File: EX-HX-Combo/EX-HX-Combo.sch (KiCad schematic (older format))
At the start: 46 parts, among them CN1 DB9 Male, J1 IDE_CONNECTOR, J200 Bus_Tandy_Plus_Through, J3 Bus_Tandy_Plus, SW1 SW_DIP_x10, U1 BIOS FLASH, U2 74HCT245, U3 1.8432 MHz, U4 DS1315, U5 AS6C4008-55PCN, U6 16550/16C550, U7 GD75232N, U8 GAL16V8, U9 GAL16V8, Y1 32.768 KHz

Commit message: Silkscreen work on EX-HX-Combo.
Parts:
- renumbered C99 to C10, C98 to C11, C10 to C12, C11 to C13, C12 to C14, C13 to C15, J3 to J2, J200 to J3
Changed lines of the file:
@@
 ~MEMR
 $Comp
-L 00Common:Bus_Tandy_Plus J3
+L 00Common:Bus_Tandy_Plus J2
 U 1 1 6039F90B
 P 2100 2750
-F 0 "J3" H 2100 4517 50  0000 C CNN
+F 0 "J2" H 2100 4517 50  0000 C CNN
 F 1 "Bus_Tandy_Plus" H 2100 4426 50  0000 C CNN
 F 2 "00Custom:TandyPlusSocket" H 2100 2750 50  0001 C CNN
@@
 UART_XIN
 $Comp
-L Device:CP C11
+L Device:CP C13
 U 1 1 60E3E53A
 P 13400 7700
-F 0 "C11" H 13518 7746 50  0000 L CNN
+F 0 "C13" H 13518 7746 50  0000 L CNN
 F 1 "100uF" H 13518 7655 50  0000 L CNN
 F 2 "Capacitor_Tantalum_SMD:CP_EIA-3528-15_AVX-H" H 13438 7550 50  0001 C CNN
@@
 $EndComp
 $Comp
-L Device:CP C12
+L Device:CP C14
 U 1 1 60D204F0
 P 13950 7700
-F 0 "C12" H 14068 7746 50  0000 L CNN
+F 0 "C14" H 14068 7746 50  0000 L CNN
 F 1 "10uF" H 14068 7655 50  0000 L CNN
 F 2 "Capacitor_Tantalum_SMD:CP_EIA-3528-15_AVX-H" H 13988 7550 50  0001 C CNN
@@
 $EndComp
 $Comp
-L Device:CP C13
+L Device:CP C15
 U 1 1 60D20522
 P 14450 7700
-F 0 "C13" H 14568 7746 50  0000 L CNN
+F 0 "C15" H 14568 7746 50  0000 L CNN
 F 1 "10uF" H 14568 7655 50  0000 L CNN
 F 2 "Capacitor_Tantalum_SMD:CP_EIA-3528-15_AVX-H" H 14488 7550 50  0001 C CNN
@@
 	5550 2850 5650 2850
 $Comp
-L 00Common:Bus_Tandy_Plus_For_Pass_Through J200
+L 00Common:Bus_Tandy_Plus_For_Pass_Through J3
 U 1 1 60D64444
 P 5050 2750
-F 0 "J200" H 5050 4517 50  0000 C CNN
+F 0 "J3" H 5050 4517 50  0000 C CNN
 F 1 "Bus_Tandy_Plus_Through" H 5050 4426 50  0000 C CNN
 F 2 "00Custom:TandyPlusSocket" H 5050 2750 50  0001 C CNN
@@
 $EndComp
 $Comp
-L Device:CP C10
+L Device:CP C12
 U 1 1 6117FB85
 P 12900 7700
-F 0 "C10" H 13018 7746 50  0000 L CNN
+F 0 "C12" H 13018 7746 50  0000 L CNN
 F 1 "100uF" H 13018 7655 50  0000 L CNN
 F 2 "Capacitor_Tantalum_SMD:CP_EIA-3528-15_AVX-H" H 12938 7550 50  0001 C CNN
@@
 $EndComp
 $Comp
-L Device:C C99
+L Device:C C10
 U 1 1 6131AD4C
 P 12050 8600
-F 0 "C99" H 12165 8646 50  0000 L CNN
+F 0 "C10" H 12165 8646 50  0000 L CNN
 F 1 "0.1uF" H 12165 8555 50  0000 L CNN
 F 2 "Capacitor_SMD:C_1206_3216Metric" H 12088 8450 50  0001 C CNN
@@
 $EndComp
 $Comp
-L Device:C C98
+L Device:C C11
 U 1 1 6143E0B4
 P 12550 8600
-F 0 "C98" H 12665 8646 50  0000 L CNN
+F 0 "C11" H 12665 8646 50  0000 L CNN
 F 1 "0.1uF" H 12665 8555 50  0000 L CNN
 F 2 "Capacitor_SMD:C_1206_3216Metric" H 12588 8450 50  0001 C CNN

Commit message: Lots of layout cleanup on EX-HX-Combo.
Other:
- note added: "MOUNTING"
- moved on the sheet: C10, C11, C12, C13, C14, C15, H1, H2, H3, H4, H5, H6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

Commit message: EX-HX-Combo: Getting close now...
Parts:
- U6: value 16550/16C550 -> 16C550
- Y1: value 32.768 KHz -> 32.768 kHz
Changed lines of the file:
@@
 P 2300 5500
 F 0 "Y1" V 2254 5631 50  0000 L CNN
-F 1 "32.768 KHz" V 2345 5631 50  0000 L CNN
+F 1 "32.768 kHz" V 2345 5631 50  0000 L CNN
 F 2 "Crystal:Crystal_C38-LF_D3.0mm_L8.0mm_Horizontal" H 2300 5500 50  0001 C CNN
 F 3 "~" H 2300 5500 50  0001 C CNN
@@
 P 2350 8850
 F 0 "U6" H 2450 10550 50  0000 C CNN
-F 1 "16550/16C550" H 2700 10450 50  0000 C CNN
+F 1 "16C550" H 2700 10450 50  0000 C CNN
 F 2 "Package_QFP:LQFP-48_7x7mm_P0.5mm" H 2350 8850 50  0001 C CIN
 F 3 "http://www.ti.com/lit/ds/symlink/pc16550d.pdf" H 2350 8850 50  0001 C CNN

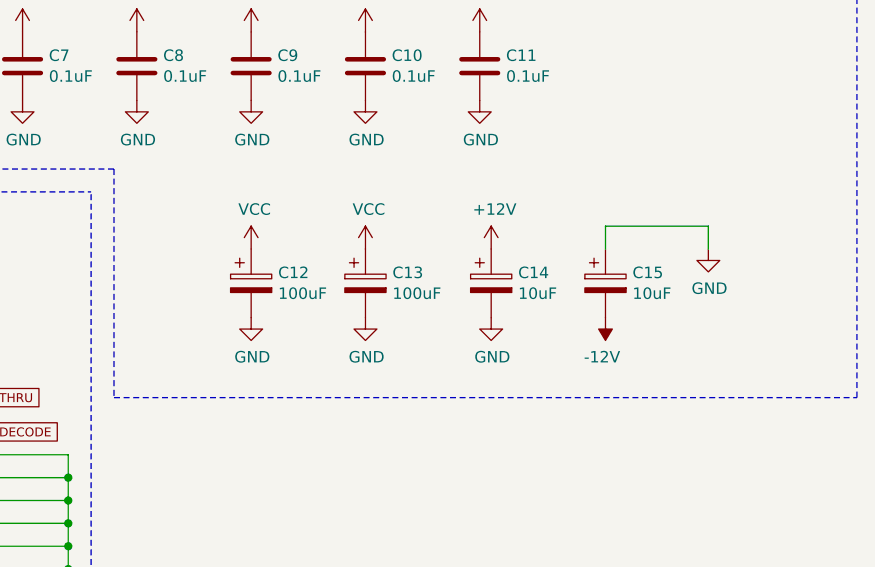
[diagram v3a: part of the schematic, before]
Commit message: EX-HX-Combo: Corrected Tantalum cap sizes, other minor changes.
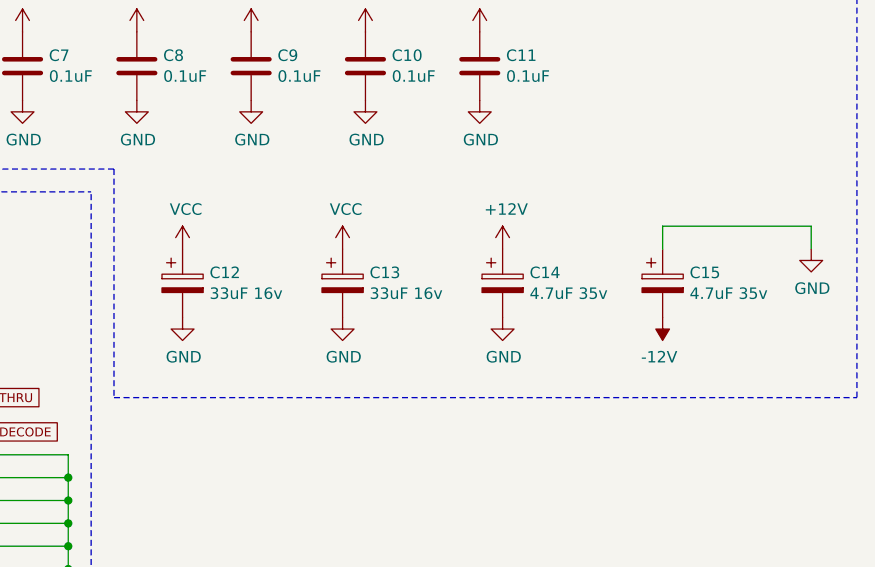
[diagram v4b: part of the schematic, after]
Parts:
- C12, C13: value 100uF -> 33uF 16v
- C14, C15: value 10uF -> 4.7uF 35v
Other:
- moved on the sheet: C12, C13, C14, C15
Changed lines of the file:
@@
 L power:VCC #PWR0121
 U 1 1 60E3DBDE
-P 12900 8500
-F 0 "#PWR0121" H 12900 8350 50  0001 C CNN
-F 1 "VCC" H 12915 8673 50  0000 C CNN
-F 2 "" H 12900 8500 50  0001 C CNN
-F 3 "" H 12900 8500 50  0001 C CNN
-	1    12900 8500
+P 12800 8500
+F 0 "#PWR0121" H 12800 8350 50  0001 C CNN
+F 1 "VCC" H 12815 8673 50  0000 C CNN
+F 2 "" H 12800 8500 50  0001 C CNN
+F 3 "" H 12800 8500 50  0001 C CNN
+	1    12800 8500
 	1    0    0    -1
 $EndComp
@@
 L power:GND #PWR0122
 U 1 1 60E3E530
-P 12900 8800
-F 0 "#PWR0122" H 12900 8550 50  0001 C CNN
-F 1 "GND" H 12905 8627 50  0000 C CNN
-F 2 "" H 12900 8800 50  0001 C CNN
-F 3 "" H 12900 8800 50  0001 C CNN
-	1    12900 8800
+P 12800 8800
+F 0 "#PWR0122" H 12800 8550 50  0001 C CNN
+F 1 "GND" H 12805 8627 50  0000 C CNN
+F 2 "" H 12800 8800 50  0001 C CNN
+F 3 "" H 12800 8800 50  0001 C CNN
+	1    12800 8800
 	1    0    0    -1
 $EndComp
@@
 Connection ~ 9100 10000
 Wire Wire Line
-	14400 8400 14400 8500
-Wire Wire Line
-	13950 8400 14400 8400
-Wire Wire Line
-	13950 8500 13950 8400
+	14850 8400 14850 8500
+Wire Wire Line
+	14200 8400 14850 8400
+Wire Wire Line
+	14200 8500 14200 8400
 $Comp
 L power:-12V #PWR0160
 U 1 1 60D20518
-P 13950 8800
-F 0 "#PWR0160" H 13950 8900 50  0001 C CNN
-F 1 "-12V" H 13965 8973 50  0000 C CNN
-F 2 "" H 13950 8800 50  0001 C CNN
-F 3 "" H 13950 8800 50  0001 C CNN
-	1    13950 8800
+P 14200 8800
+F 0 "#PWR0160" H 14200 8900 50  0001 C CNN
+F 1 "-12V" H 14215 8973 50  0000 C CNN
+F 2 "" H 14200 8800 50  0001 C CNN
+F 3 "" H 14200 8800 50  0001 C CNN
+	1    14200 8800
 	-1   0    0    1
 $EndComp
@@
 L power:+12V #PWR0159
 U 1 1 60D2050E
-P 13450 8500
-F 0 "#PWR0159" H 13450 8350 50  0001 C CNN
-F 1 "+12V" H 13465 8673 50  0000 C CNN
-F 2 "" H 13450 8500 50  0001 C CNN
-F 3 "" H 13450 8500 50  0001 C CNN
-	1    13450 8500
+P 13500 8500
+F 0 "#PWR0159" H 13500 8350 50  0001 C CNN
+F 1 "+12V" H 13515 8673 50  0000 C CNN
+F 2 "" H 13500 8500 50  0001 C CNN
+F 3 "" H 13500 8500 50  0001 C CNN
+	1    13500 8500
 	1    0    0    -1
 $EndComp
@@
 L power:GND #PWR0158
 U 1 1 60D20504
-P 14400 8500
-F 0 "#PWR0158" H 14400 8250 50  0001 C CNN
-F 1 "GND" H 14405 8327 50  0000 C CNN
-F 2 "" H 14400 8500 50  0001 C CNN
-F 3 "" H 14400 8500 50  0001 C CNN
-	1    14400 8500
+P 14850 8500
+F 0 "#PWR0158" H 14850 8250 50  0001 C CNN
+F 1 "GND" H 14855 8327 50  0000 C CNN
+F 2 "" H 14850 8500 50  0001 C CNN
+F 3 "" H 14850 8500 50  0001 C CNN
+	1    14850 8500
 	1    0    0    -1
 $EndComp
@@
 L power:GND #PWR0157
 U 1 1 60D204FA
-P 13450 8800
-F 0 "#PWR0157" H 13450 8550 50  0001 C CNN
-F 1 "GND" H 13455 8627 50  0000 C CNN
-F 2 "" H 13450 8800 50  0001 C CNN
-F 3 "" H 13450 8800 50  0001 C CNN
-	1    13450 8800
+P 13500 8800
+F 0 "#PWR0157" H 13500 8550 50  0001 C CNN
+F 1 "GND" H 13505 8627 50  0000 C CNN
+F 2 "" H 13500 8800 50  0001 C CNN
+F 3 "" H 13500 8800 50  0001 C CNN
+	1    13500 8800
 	1    0    0    -1
 $EndComp
@@
 L Device:CP C13
 U 1 1 60E3E53A
-P 12900 8650
-F 0 "C13" H 13018 8696 50  0000 L CNN
-F 1 "100uF" H 13018 8605 50  0000 L CNN
-F 2 "Capacitor_Tantalum_SMD:CP_EIA-3528-15_AVX-H" H 12938 8500 50  0001 C CNN
-F 3 "~" H 12900 8650 50  0001 C CNN
-	1    12900 8650
+P 12800 8650
+F 0 "C13" H 12918 8696 50  0000 L CNN
+F 1 "33uF 16v" H 12918 8605 50  0000 L CNN
+F 2 "Capacitor_Tantalum_SMD:CP_EIA-3528-15_AVX-H" H 12838 8500 50  0001 C CNN
+F 3 "~" H 12800 8650 50  0001 C CNN
+	1    12800 8650
 	1    0    0    -1
 $EndComp
@@
 L Device:CP C14
 U 1 1 60D204F0
-P 13450 8650
-F 0 "C14" H 13568 8696 50  0000 L CNN
-F 1 "10uF" H 13568 8605 50  0000 L CNN
-F 2 "Capacitor_Tantalum_SMD:CP_EIA-3528-15_AVX-H" H 13488 8500 50  0001 C CNN
-F 3 "~" H 13450 8650 50  0001 C CNN
-	1    13450 8650
+P 13500 8650
+F 0 "C14" H 13618 8696 50  0000 L CNN
+F 1 "4.7uF 35v" H 13618 8605 50  0000 L CNN
+F 2 "Capacitor_Tantalum_SMD:CP_EIA-3528-15_AVX-H" H 13538 8500 50  0001 C CNN
+F 3 "~" H 13500 8650 50  0001 C CNN
+	1    13500 8650
 	1    0    0    -1
 $EndComp
@@
 L Device:CP C15
 U 1 1 60D20522
-P 13950 8650
-F 0 "C15" H 14068 8696 50  0000 L CNN
-F 1 "10uF" H 14068 8605 50  0000 L CNN
-F 2 "Capacitor_Tantalum_SMD:CP_EIA-3528-15_AVX-H" H 13988 8500 50  0001 C CNN
-F 3 "~" H 13950 8650 50  0001 C CNN
-	1    13950 8650
+P 14200 8650
+F 0 "C15" H 14318 8696 50  0000 L CNN
+F 1 "4.7uF 35v" H 14318 8605 50  0000 L CNN
+F 2 "Capacitor_Tantalum_SMD:CP_EIA-3528-15_AVX-H" H 14238 8500 50  0001 C CNN
+F 3 "~" H 14200 8650 50  0001 C CNN
+	1    14200 8650
 	1    0    0    -1
 $EndComp
@@
 L power:VCC #PWR0171
 U 1 1 6117F173
-P 12400 8500
-F 0 "#PWR0171" H 12400 8350 50  0001 C CNN
-F 1 "VCC" H 12415 8673 50  0000 C CNN
-F 2 "" H 12400 8500 50  0001 C CNN
-F 3 "" H 12400 8500 50  0001 C CNN
-	1    12400 8500
+P 12100 8500
+F 0 "#PWR0171" H 12100 8350 50  0001 C CNN
+F 1 "VCC" H 12115 8673 50  0000 C CNN
+F 2 "" H 12100 8500 50  0001 C CNN
+F 3 "" H 12100 8500 50  0001 C CNN
+	1    12100 8500
 	1    0    0    -1
 $EndComp
@@
 L power:GND #PWR0172
 U 1 1 6117FB7B
-P 12400 8800
-F 0 "#PWR0172" H 12400 8550 50  0001 C CNN
-F 1 "GND" H 12405 8627 50  0000 C CNN
-F 2 "" H 12400 8800 50  0001 C CNN
-F 3 "" H 12400 8800 50  0001 C CNN
-	1    12400 8800
+P 12100 8800
+F 0 "#PWR0172" H 12100 8550 50  0001 C CNN
+F 1 "GND" H 12105 8627 50  0000 C CNN
+F 2 "" H 12100 8800 50  0001 C CNN
+F 3 "" H 12100 8800 50  0001 C CNN
+	1    12100 8800
 	1    0    0    -1
 $EndComp
@@
 L Device:CP C12
 U 1 1 6117FB85
-P 12400 8650
-F 0 "C12" H 12518 8696 50  0000 L CNN
-F 1 "100uF" H 12518 8605 50  0000 L CNN
-F 2 "Capacitor_Tantalum_SMD:CP_EIA-3528-15_AVX-H" H 12438 8500 50  0001 C CNN
-F 3 "~" H 12400 8650 50  0001 C CNN
-	1    12400 8650
-	1    0    0    -1
-$EndComp
+P 12100 8650
+F 0 "C12" H 12218 8696 50  0000 L CNN
+F 1 "33uF 16v" H 12218 8605 50  0000 L CNN
+F 2 "Capacitor_Tantalum_SMD:CP_EIA-3528-15_AVX-H" H 12138 8500 50  0001 C CNN
+F 3 "~" H 12100 8650 50  0001 C CNN
+	1    12100 8650
+	1    0    0    -1
+$EndComp

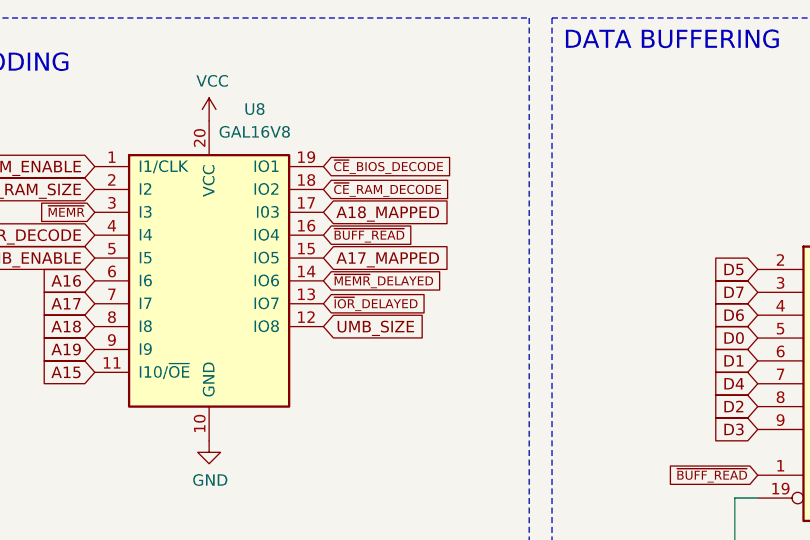
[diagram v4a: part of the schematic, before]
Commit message: EX-HX-Combo: Updated GAL logic to match current pinouts. Needed to reorder some pins on MemLogic due to logic compile errors.
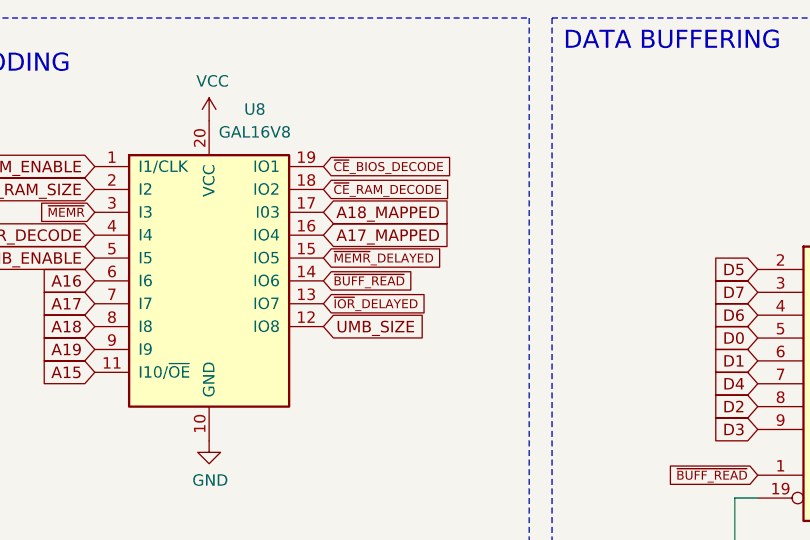
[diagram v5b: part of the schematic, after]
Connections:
- net A17_MAPPED: now also U8.16 (IO4); no longer U8.15 (IO5)
- net ~BUFF_READ: now also U8.14 (IO6); no longer U8.16 (IO4)
- net ~MEMR~_DELAYED: now also U8.15 (IO5); no longer U8.14 (IO6)
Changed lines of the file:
@@
 	1    0    0    -1
 $EndComp
-Text GLabel 8200 1550 2    39   Input ~ 0
+Text GLabel 8200 1750 2    39   Input ~ 0
 ~BUFF_READ
 Text GLabel 7200 3500 0    39   Input ~ 0
@@
 Wire Notes Line
 	15050 600  15050 4050
-Text GLabel 8200 1750 2    39   Input ~ 0
+Text GLabel 8200 1650 2    39   Input ~ 0
 ~MEMR~_DELAYED
 $Comp
@@
 Text GLabel 8200 1350 2    39   Input ~ 0
 ~CE~_RAM_DECODE
-Text GLabel 8200 1650 2    50   Input ~ 0
-A17_MAPPED
 Text GLabel 8200 3500 2    50   Input ~ 0
 IOR_DECODE
@@
 Wire Notes Line
 	8200 7150 8200 8150
+Text GLabel 8200 1550 2    50   Input ~ 0
+A17_MAPPED
 $EndSCHEMATC

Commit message: EX-HX-Combo: More work preparing for JLCPCB assembly.
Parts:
- BAT1: LCSC (none) -> C964758; Part options (none) -> C964756, C964758, C964764, C964762, C70377, C964760
- C1, C10, C11, C2, C3, C4, C5, C6, C7, C8, C9: LCSC (none) -> C24497
- R1, R2, R3, R4, R5, R6, R7: LCSC (none) -> C17902
- U1, U5: LCSC (none) -> C146583; Part options (none) -> C72122, C146583, C2331
- U2, U8, U9: LCSC (none) -> C72118; Part options (none) -> C72118, C132507, C2328
- U3: LCSC (none) -> C386895
- U4: LCSC (none) -> C72115; Part options (none) -> C72115, C146580, C2326
- U6: LCSC (none) -> C181382; Part options (none) -> C181382, C2692304, C84320, C352984
- U7: value GD75232N -> GD75232; LCSC (none) -> C6662
- Y1: LCSC (none) -> C182062; Part options (none) -> C182062, C127496
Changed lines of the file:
@@
 F 3 "http://ww1.microchip.com/downloads/en/DeviceDoc/25022B.pdf" H 13850 2700 50  0001 C CNN
 F 4 "SST39SF010, SST39SF020, SST39SF040 or similar" H 13850 3789 50  0000 C CNN "Note"
+F 5 "C146583" H 13850 2400 50  0001 C CNN "LCSC"
+F 6 "C72122, C146583, C2331" H 13850 2400 50  0001 C CNN "Part options"
 	1    13850 2400
 	1    0    0    -1
@@
 F 2 "Capacitor_SMD:C_1206_3216Metric" H 8388 7550 50  0001 C CNN
 F 3 "~" H 8350 7700 50  0001 C CNN
+F 4 " C24497" H 8350 7700 50  0001 C CNN "LCSC"
 	1    8350 7700
 	1    0    0    -1
@@
 F 2 "Capacitor_SMD:C_1206_3216Metric" H 8888 7550 50  0001 C CNN
 F 3 "~" H 8850 7700 50  0001 C CNN
+F 4 " C24497" H 8850 7700 50  0001 C CNN "LCSC"
 	1    8850 7700
 	1    0    0    -1
@@
 F 2 "Package_DIP:DIP-20_W7.62mm_Socket" H 10600 2200 50  0001 C CNN
 F 3 "http://www.ti.com/lit/gpn/sn74LS245" H 10600 2200 50  0001 C CNN
+F 4 "C72118" H 10600 2200 50  0001 C CNN "LCSC"
+F 5 "C72118, C132507, C2328" H 10600 2200 50  0001 C CNN "Part options"
 	1    10600 2200
 	1    0    0    -1
@@
 F 2 "Battery:BatteryHolder_Keystone_1060_1x2032" V 2300 6310 50  0001 C CNN
 F 3 "~" V 2300 6310 50  0001 C CNN
+F 4 "C964758" H 2300 6250 50  0001 C CNN "LCSC"
+F 5 "C964756, C964758, C964764, C964762, C70377, C964760" H 2300 6250 50  0001 C CNN "Part options"
 	1    2300 6250
 	1    0    0    -1
@@
 F 2 "Crystal:Crystal_C38-LF_D3.0mm_L8.0mm_Horizontal" H 2300 5500 50  0001 C CNN
 F 3 "~" H 2300 5500 50  0001 C CNN
+F 4 "C182062" V 2300 5500 50  0001 C CNN "LCSC"
+F 5 "C182062, C127496" V 2300 5500 50  0001 C CNN "Part options"
 	1    2300 5500
 	0    1    1    0
@@
 F 2 "Package_DIP:DIP-16_W7.62mm_Socket" H 3800 5450 50  0001 C CNN
 F 3 "" H 3800 5450 50  0001 C CNN
+F 4 "C72115" H 3800 5450 50  0001 C CNN "LCSC"
+F 5 "C72115, C146580, C2326" H 3800 5450 50  0001 C CNN "Part options"
 	1    3800 5450
 	1    0    0    -1
@@
 F 2 "Package_DIP:DIP-32_W15.24mm_Socket" H 13650 5700 50  0001 C CNN
 F 3 "https://www.alliancememory.com/wp-content/uploads/pdf/AS6C4008.pdf" H 13650 5700 50  0001 C CNN
+F 4 "C146583" H 13650 5600 50  0001 C CNN "LCSC"
+F 5 "C72122, C146583, C2331" H 13650 5600 50  0001 C CNN "Part options"
 	1    13650 5600
 	1    0    0    -1
@@
 F 2 "Capacitor_SMD:C_1206_3216Metric" H 10388 7550 50  0001 C CNN
 F 3 "~" H 10350 7700 50  0001 C CNN
+F 4 " C24497" H 10350 7700 50  0001 C CNN "LCSC"
 	1    10350 7700
 	1    0    0    -1
@@
 F 2 "Capacitor_SMD:C_1206_3216Metric" H 9888 7550 50  0001 C CNN
 F 3 "~" H 9850 7700 50  0001 C CNN
+F 4 " C24497" H 9850 7700 50  0001 C CNN "LCSC"
 	1    9850 7700
 	1    0    0    -1
@@
 F 2 "Capacitor_SMD:C_1206_3216Metric" H 9388 7550 50  0001 C CNN
 F 3 "~" H 9350 7700 50  0001 C CNN
+F 4 " C24497" H 9350 7700 50  0001 C CNN "LCSC"
 	1    9350 7700
 	1    0    0    -1
@@
 P 4850 8050
 F 0 "U7" H 5100 8750 50  0000 C CNN
-F 1 "GD75232N" H 5200 8650 50  0000 C CNN
+F 1 "GD75232" H 5200 8650 50  0000 C CNN
 F 2 "Package_SO:SOIC-20W_7.5x12.8mm_P1.27mm" H 4850 7250 50  0001 C CIN
 F 3 "http://www.ti.com/lit/ds/symlink/gd75232.pdf" H 4350 8050 50  0001 C CNN
+F 4 "C6662" H 4850 8050 50  0001 C CNN "LCSC"
 	1    4850 8050
 	1    0    0    -1
@@
 F 2 "Capacitor_SMD:C_1206_3216Metric" H 11438 7550 50  0001 C CNN
 F 3 "~" H 11400 7700 50  0001 C CNN
+F 4 " C24497" H 11400 7700 50  0001 C CNN "LCSC"
 	1    11400 7700
 	1    0    0    -1
@@
 F 2 "Capacitor_SMD:C_1206_3216Metric" H 11938 7550 50  0001 C CNN
 F 3 "~" H 11900 7700 50  0001 C CNN
+F 4 " C24497" H 11900 7700 50  0001 C CNN "LCSC"
 	1    11900 7700
 	1    0    0    -1
@@
 F 2 "Capacitor_SMD:C_1206_3216Metric" H 12438 7550 50  0001 C CNN
 F 3 "~" H 12400 7700 50  0001 C CNN
+F 4 " C24497" H 12400 7700 50  0001 C CNN "LCSC"
 	1    12400 7700
 	1    0    0    -1
@@
 F 2 "Capacitor_SMD:C_1206_3216Metric" H 10888 7550 50  0001 C CNN
 F 3 "~" H 10850 7700 50  0001 C CNN
+F 4 " C24497" H 10850 7700 50  0001 C CNN "LCSC"
 	1    10850 7700
 	1    0    0    -1
@@
 F 2 "Package_DIP:DIP-20_W7.62mm_Socket" H 7700 1750 50  0001 C CNN
 F 3 "" H 7700 1750 50  0001 C CNN
+F 4 "C72118" H 7700 1750 50  0001 C CNN "LCSC"
+F 5 "C72118, C132507, C2328" H 7700 1750 50  0001 C CNN "Part options"
 	1    7700 1750
 	1    0    0    -1
@@
 F 2 "Package_DIP:DIP-20_W7.62mm_Socket" H 7700 3800 50  0001 C CNN
 F 3 "" H 7700 3800 50  0001 C CNN
+F 4 "C72118" H 7700 3800 50  0001 C CNN "LCSC"
+F 5 "C72118, C132507, C2328" H 7700 3800 50  0001 C CNN "Part options"
 	1    7700 3800
 	1    0    0    -1
@@
 F 2 "Resistor_SMD:R_1206_3216Metric" V 9030 9050 50  0001 C CNN
 F 3 "~" H 9100 9050 50  0001 C CNN
+F 4 "C17902" V 9100 9050 50  0001 C CNN "LCSC"
 	1    9100 9050
 	1    0    0    -1
@@
 F 2 "Resistor_SMD:R_1206_3216Metric" V 9430 9050 50  0001 C CNN
 F 3 "~" H 9500 9050 50  0001 C CNN
+F 4 "C17902" V 9500 9050 50  0001 C CNN "LCSC"
 	1    9500 9050
 	1    0    0    -1
@@
 F 2 "Resistor_SMD:R_1206_3216Metric" V 9230 9050 50  0001 C CNN
 F 3 "~" H 9300 9050 50  0001 C CNN
+F 4 "C17902" V 9300 9050 50  0001 C CNN "LCSC"
 	1    9300 9050
 	1    0    0    -1
@@
 F 2 "Resistor_SMD:R_1206_3216Metric" V 9630 9050 50  0001 C CNN
 F 3 "~" H 9700 9050 50  0001 C CNN
+F 4 "C17902" V 9700 9050 50  0001 C CNN "LCSC"
 	1    9700 9050
 	1    0    0    -1
@@
 F 2 "Resistor_SMD:R_1206_3216Metric" V 10030 9050 50  0001 C CNN
 F 3 "~" H 10100 9050 50  0001 C CNN
+F 4 "C17902" V 10100 9050 50  0001 C CNN "LCSC"
 	1    10100 9050
 	1    0    0    -1
@@
 Wire Wire Line
 	7250 5950 7150 5950
-$Comp
-L Oscillator:SG-7050CAN U3
-U 1 1 6125B3CC
-P 7550 5950
-F 0 "U3" H 7650 6300 50  0000 L CNN
-F 1 "1.8432 MHz" H 7650 6200 50  0000 L CNN
-F 2 "Oscillator:Oscillator_SMD_SeikoEpson_SG8002CA-4Pin_7.0x5.0mm" H 8250 5600 50  0001 C CNN
-F 3 "https://support.epson.biz/td/api/doc_check.php?dl=brief_SG7050CAN&lang=en" H 7450 5950 50  0001 C CNN
-	1    7550 5950
-	1    0    0    -1
-$EndComp
 Wire Wire Line
 	7150 5650 7150 5950
@@
 F 2 "Package_QFP:LQFP-48_7x7mm_P0.5mm" H 2350 8850 50  0001 C CIN
 F 3 "http://www.ti.com/lit/ds/symlink/pc16550d.pdf" H 2350 8850 50  0001 C CNN
+F 4 "C181382" H 2350 8850 50  0001 C CNN "LCSC"
+F 5 "C181382, C2692304, C84320, C352984" H 2350 8850 50  0001 C CNN "Part options"
 	1    2350 8850
 	1    0    0    -1
@@
 F 2 "Capacitor_SMD:C_1206_3216Metric" H 12938 7550 50  0001 C CNN
 F 3 "~" H 12900 7700 50  0001 C CNN
+F 4 " C24497" H 12900 7700 50  0001 C CNN "LCSC"
 	1    12900 7700
 	1    0    0    -1
@@
 F 2 "Capacitor_SMD:C_1206_3216Metric" H 13438 7550 50  0001 C CNN
 F 3 "~" H 13400 7700 50  0001 C CNN
+F 4 " C24497" H 13400 7700 50  0001 C CNN "LCSC"
 	1    13400 7700
 	1    0    0    -1
@@
 F 2 "Resistor_SMD:R_1206_3216Metric" V 10230 9050 50  0001 C CNN
 F 3 "~" H 10300 9050 50  0001 C CNN
+F 4 "C17902" V 10300 9050 50  0001 C CNN "LCSC"
 	1    10300 9050
 	1    0    0    -1
@@
 F 2 "Resistor_SMD:R_1206_3216Metric" V 9830 9050 50  0001 C CNN
 F 3 "~" H 9900 9050 50  0001 C CNN
+F 4 "C17902" V 9900 9050 50  0001 C CNN "LCSC"
 	1    9900 9050
 	1    0    0    -1
@@
 Text GLabel 8200 1550 2    50   Input ~ 0
 A17_MAPPED
+$Comp
+L Oscillator:SG-7050CAN U3
+U 1 1 6125B3CC
+P 7550 5950
+F 0 "U3" H 7650 6300 50  0000 L CNN
+F 1 "1.8432 MHz" H 7650 6200 50  0000 L CNN
+F 2 "Oscillator:Oscillator_SMD_SeikoEpson_SG8002CA-4Pin_7.0x5.0mm" H 8250 5600 50  0001 C CNN
+F 3 "https://support.epson.biz/td/api/doc_check.php?dl=brief_SG7050CAN&lang=en" H 7450 5950 50  0001 C CNN
+F 4 "C386895" H 7550 5950 50  0001 C CNN "LCSC"
+	1    7550 5950
+	1    0    0    -1
+$EndComp
 $EndSCHEMATC
